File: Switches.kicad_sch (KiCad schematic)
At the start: 24 parts, among them J2 Supp_In, J3 Supp_Out

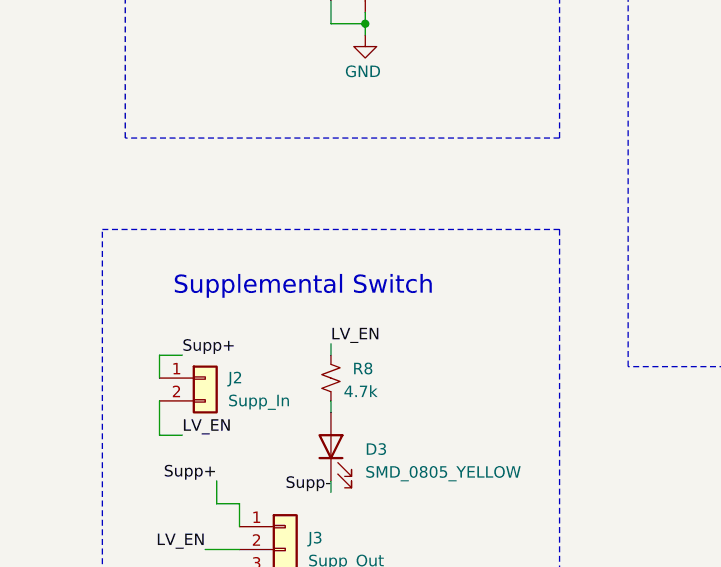
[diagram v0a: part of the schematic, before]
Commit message: Changed from Internal CAN to Peripheral CAN
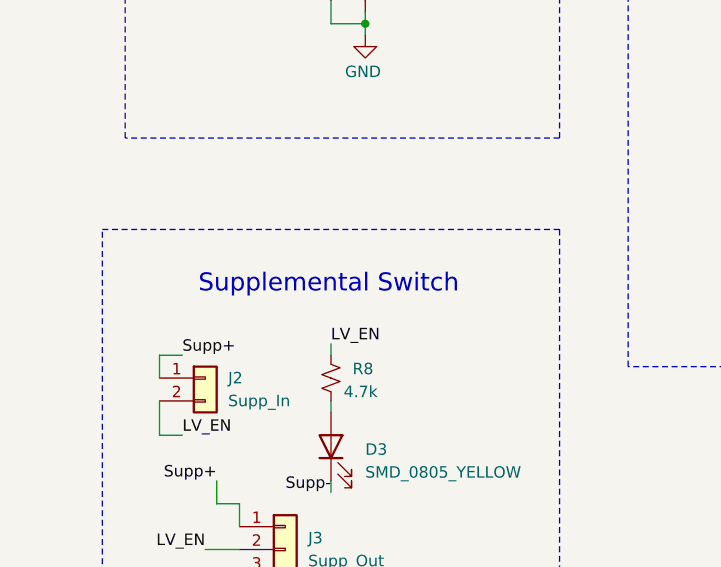
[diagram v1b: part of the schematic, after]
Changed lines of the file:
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@@
 	(text "Supplemental Switch"
 		(exclude_from_sim no)
-		(at 45.212 95.25 0)
+		(at 48.006 94.996 0)
 		(effects
 			(font
